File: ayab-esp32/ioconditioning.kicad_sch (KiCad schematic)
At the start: 45 parts, among them J701 CTRL_3v3, J702 CTRL_5V, U702 LM393, U703 LM393

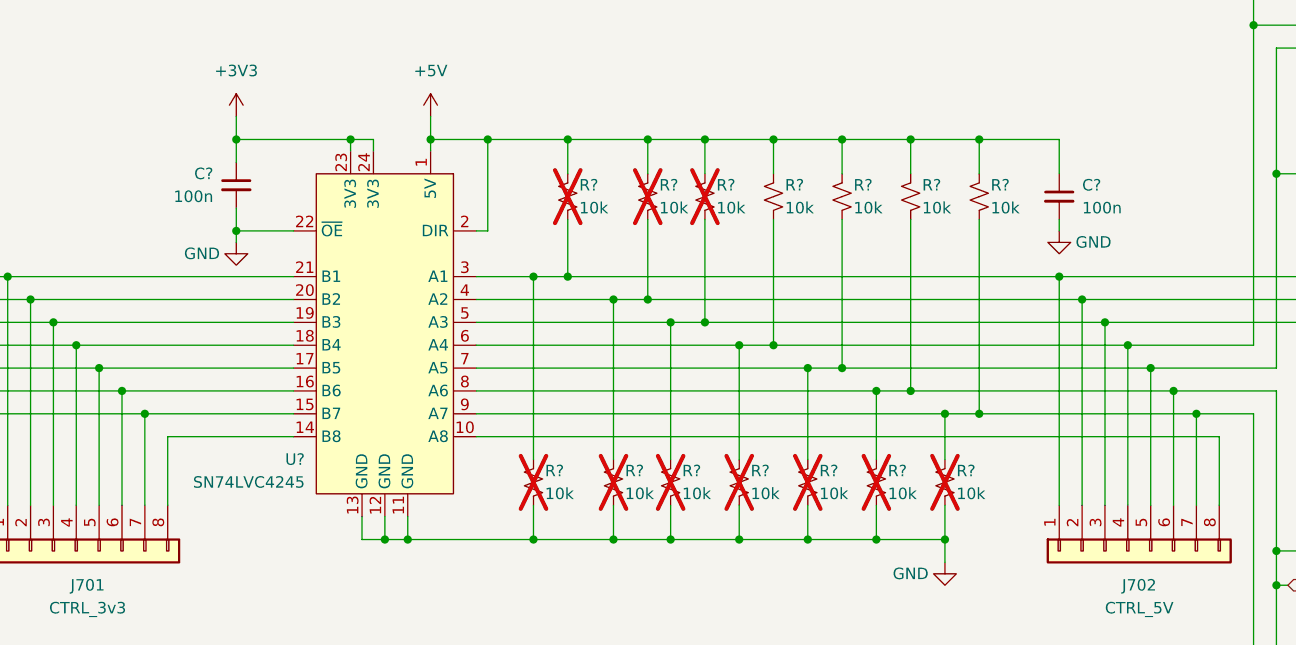
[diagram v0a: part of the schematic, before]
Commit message: revise connector positions
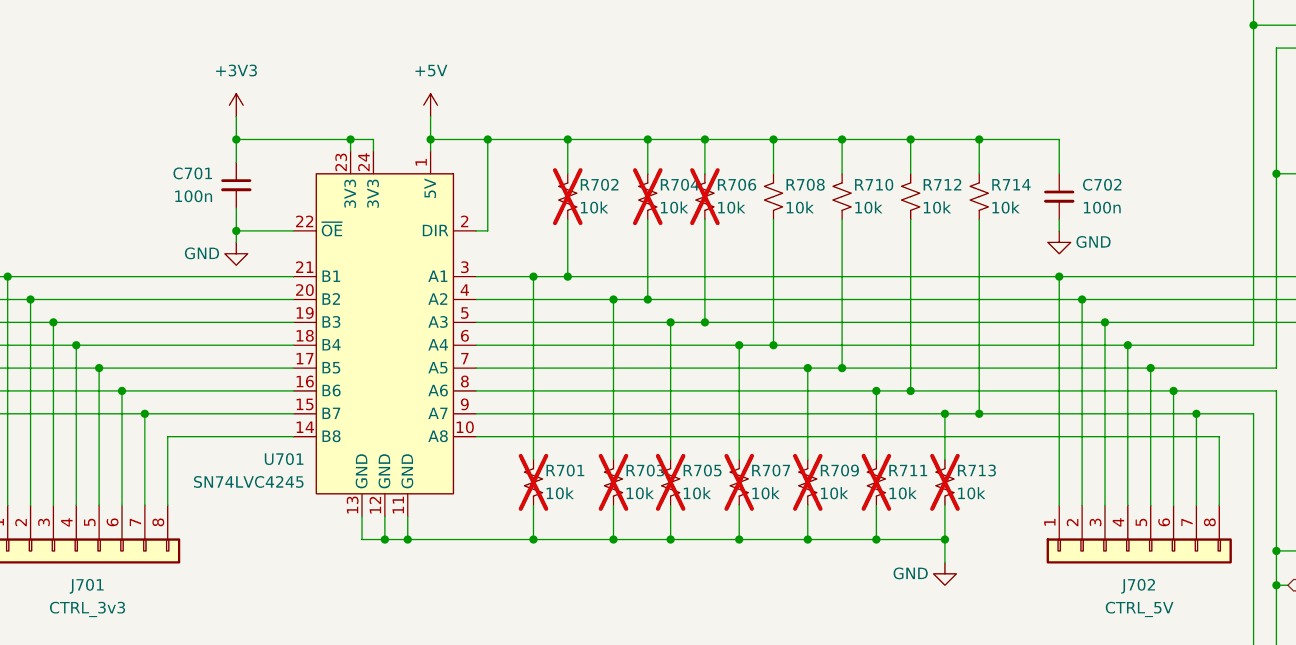
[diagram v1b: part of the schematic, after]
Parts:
- J701, J702: LCSC ID (none) -> C225519; OEM (none) -> CJT(Changjiang Connectors); OEM PN (none) -> A2541WV-2x4P
- U702, U703: LCSC ID (none) -> C7955
- gave numbers to parts that had none: 17

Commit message: Correct footprint and regenerate documentation
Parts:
- U701: footprint Package_SO:TSSOP-24_4.4x6.5mm_P0.5mm -> Package_SO:TSSOP-24_4.4x7.8mm_P0.65mm
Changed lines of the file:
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@@
       (effects (font (size 1.27 1.27)) (justify left))
     )
-    (property "Footprint" "Package_SO:TSSOP-24_4.4x6.5mm_P0.5mm" (at 81.28 119.38 0)
+    (property "Footprint" "Package_SO:TSSOP-24_4.4x7.8mm_P0.65mm" (at 81.28 119.38 0)
       (effects (font (size 1.27 1.27)) hide)
     )

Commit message: add mouser parts list
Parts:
- C701, C702, C703, C704: Mouser PN (none) -> 187-CL10B104MB8NNNC
- J701, J702: Mouser PN (none) -> 649-67997-108HLF
- R701, R702, R703, R704, R705, R706, R707, R708, R709, R710, R711, R712, R713, R714, R719, R720, R721, R722: Mouser PN (none) -> 791-RMC16K103FTP
- R715, R716, R717, R718: Mouser PN (none) -> 71-CRCW0603100KJNEAC
- R723, R725, R728, R730: Mouser PN (none) -> 71-CRCW06034K70FKEAC
- R724, R726: Mouser PN (none) -> 71-CRCW06031K24FKEAC
- R727, R729: Mouser PN (none) -> 603-RC0603FR-073K3P
- R731, R732: Mouser PN (none) -> 603-RC0603JR-0722KL
- R733, R734: Mouser PN (none) -> 603-AC0603FR-1047KL
- U701: Mouser PN (none) -> 595-SN74LVC4245APWRG
- U702, U703: Mouser PN (none) -> 926-LM393M/NOPB
